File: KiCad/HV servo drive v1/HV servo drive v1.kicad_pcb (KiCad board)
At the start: 4 copper layers, 138.4 x 199.6 mm, 323 parts, among them J10 DC BUS J2, J3 PROG, J5 MOTOR, J6 PFC SENSE, J7 DC BUS J1, J8 8P8C_LED_Shielded_x2, J9 Conn_02x03_Top_Bottom, M1 Fan_4pin, M2 Fan_4pin, Q1 C3M0075120K, Q2 C3M0075120K, Q3 C3M0075120K, Q4 C3M0075120K, Q5 C3M0075120K, Q6 C3M0075120K, Q8 PMOS, SW1 SW_DIP_x04, SW2 TERM RES, U1 TCA9555PWR, U10 2EDF9275FXUMA1, U11 2EDF9275FXUMA1, U12 AMC1306M25DWVR, U13 2EDF9275FXUMA1, U14 AMC1306M25DWVR, U15 AMC1306M25DWVR, U16 6N137, U17 6N137, U18 FODM217A, U19 FODM217A, U2 ISO6721BQDRQ1, U20 WRF0505S-3WR2, U21 B0505MT-1WR4, U22 PL133-37TC, U23 THVD1552, U3 ISO6721BQDRQ1, U4 ISO6721BQDRQ1, U6 AP64060QWU-7, U7 WRF0505S-3WR2, U8 B0505MT-1WR4, U9 AP2127K-3.3, U9 STM32F413RGT6

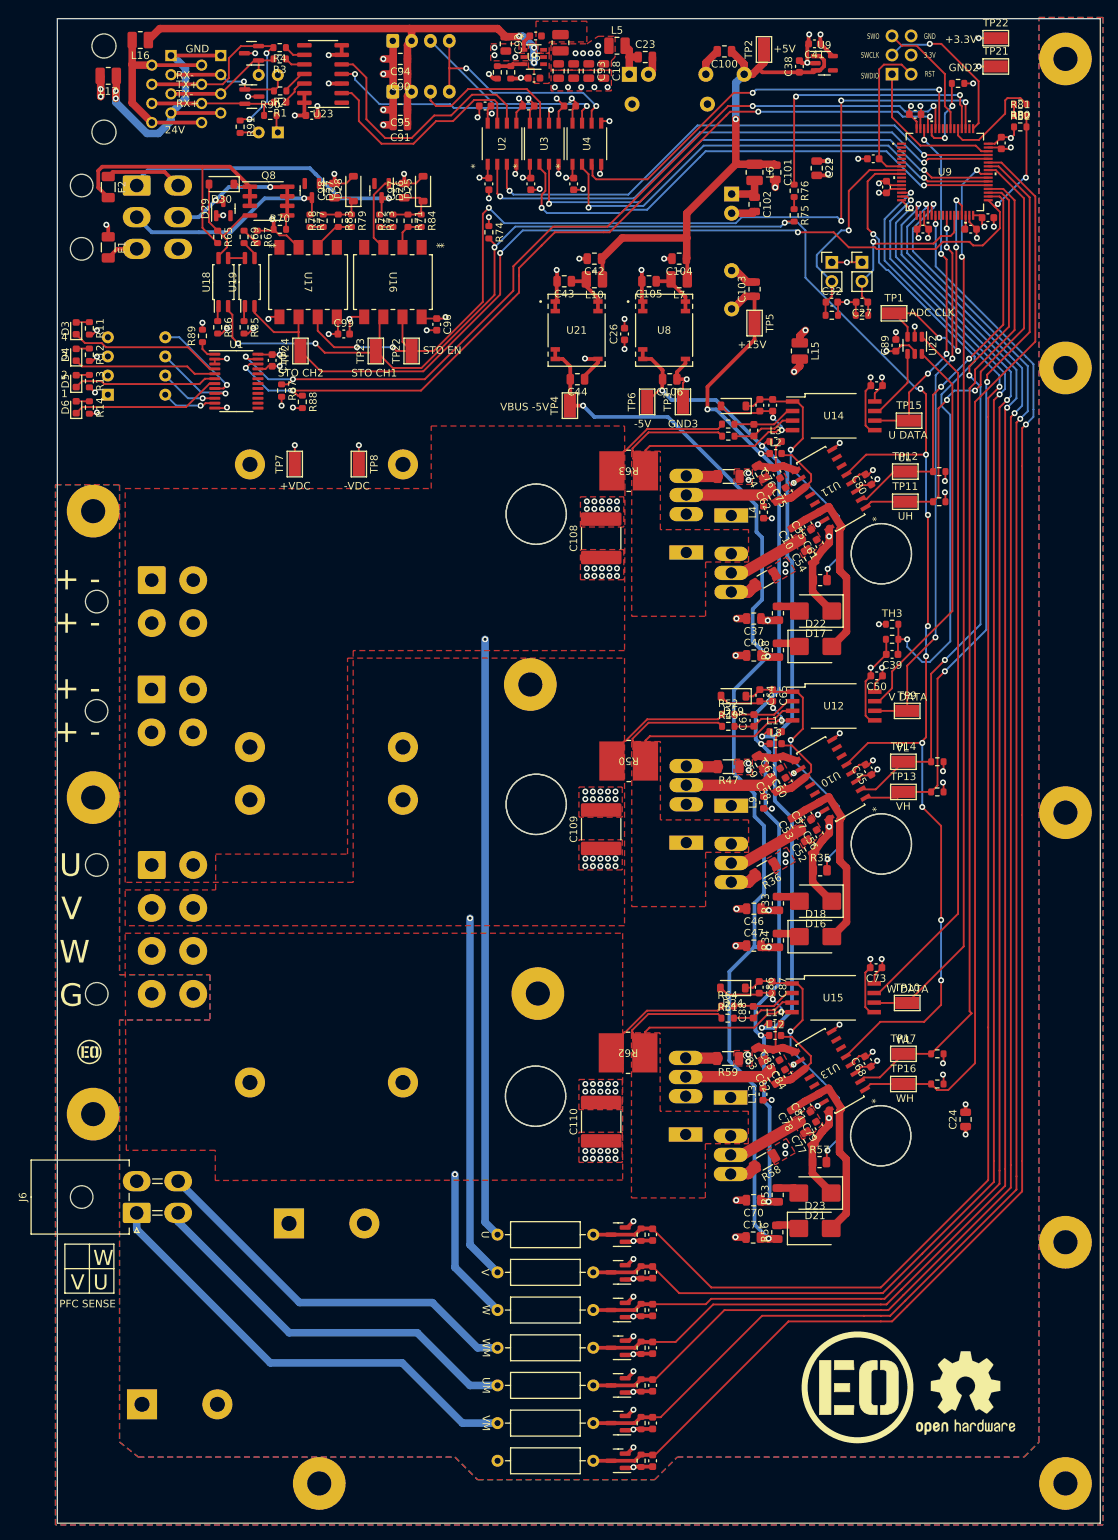
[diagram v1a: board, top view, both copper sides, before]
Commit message: start rev 2 changes
fix component references, fix rj45 and dc-dc converter footprints, add RLC filters on all power connectors, add more mounting holes
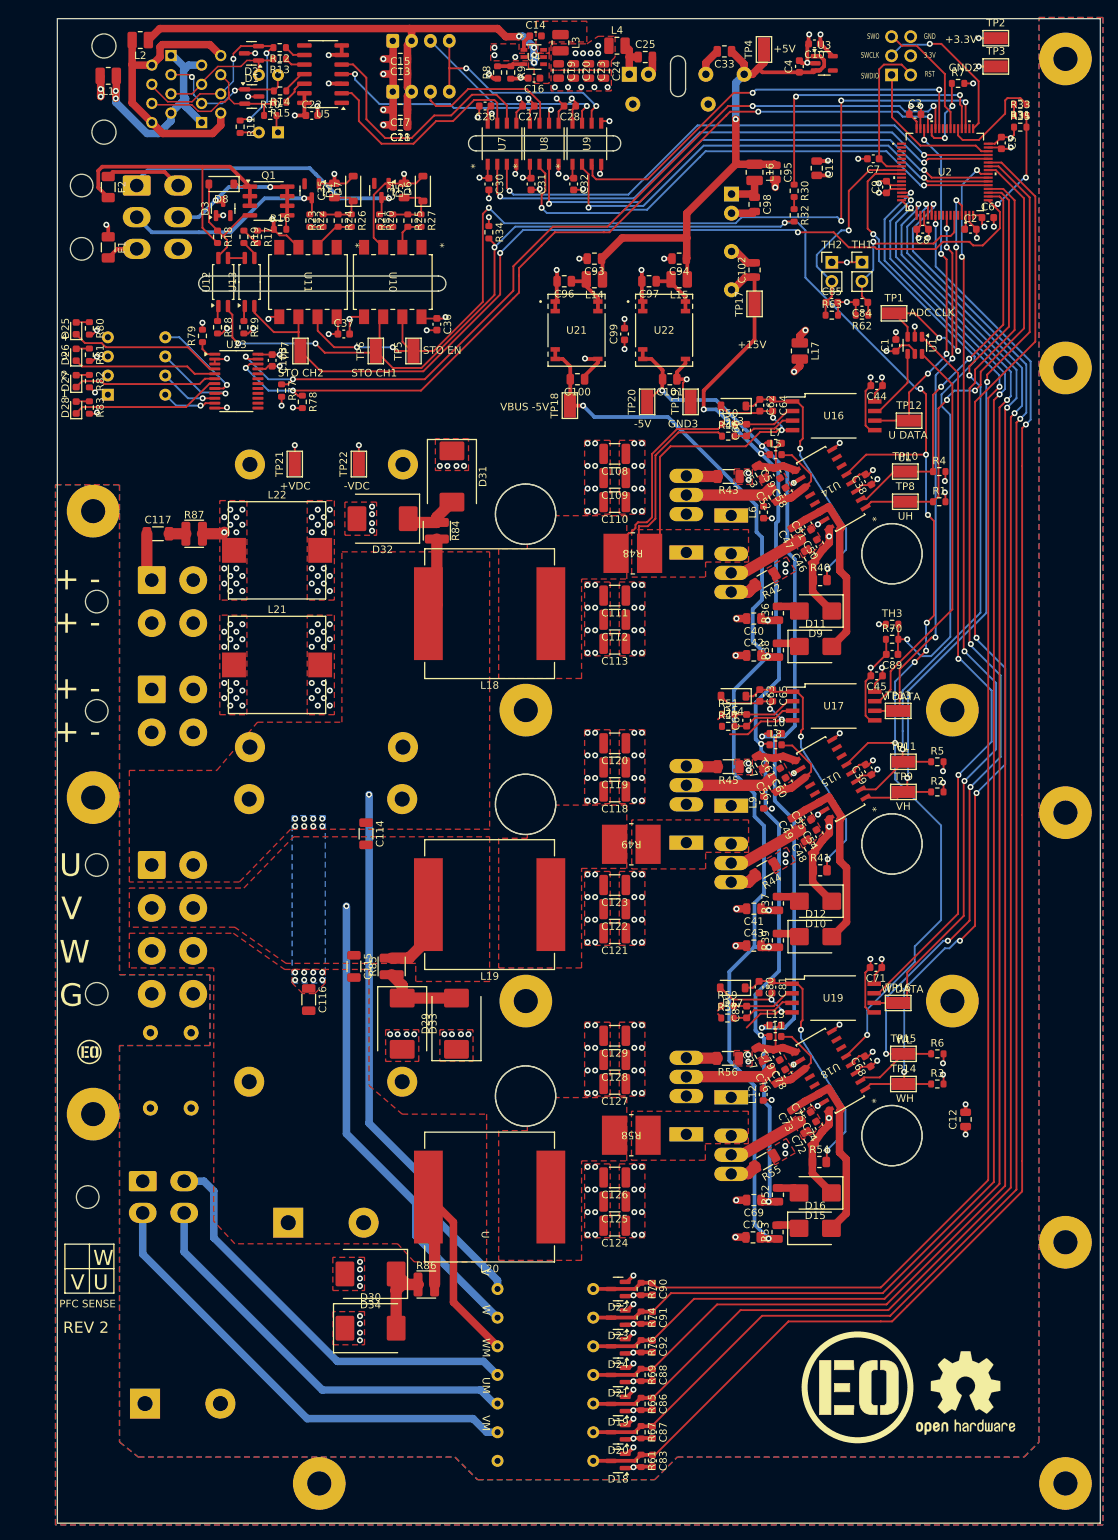
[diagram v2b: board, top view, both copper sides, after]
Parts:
- removed H14: MountingHole, footprints:MountingHole_3.2mm_M3_Pad_TopBottom_LargeIsolation
- removed J10: DC BUS J2, Connector_Molex:Molex_Mega-Fit_76825-0004_2x02_P5.70mm_Horizontal
- removed J8: 8P8C_LED_Shielded_x2, footprints:RJ45_E5908-0T0343-L
- removed J9: Conn_02x03_Top_Bottom, Connector_Molex:Molex_Mini-Fit_Jr_5569-06A2_2x03_P4.20mm_Horizontal
- removed Q8: PMOS, Package_SO:SOIC-8_3.9x4.9mm_P1.27mm
- removed R88, R89: 10k, Resistor_SMD:R_0603_1608Metric
- removed R90, R91: 120, Resistor_SMD:R_0603_1608Metric
- removed the REF** at (314.5, 188.8)
- removed the TP2 at (404.0, 55.8)
- removed TP23, TP24: TestPoint, footprints:TestPoint_Pad_3.1x1.6mm
- removed the TP3 at (393.2, 102.5)
- removed the U9 at (412.0, 57.6)
- removed the U9 at (428.0, 72.0)
- added C111: C, Capacitor_SMD:C_1210_3225Metric, F.Cu at (384.2, 128.2)
- added C112: C, Capacitor_SMD:C_1210_3225Metric, F.Cu at (384.2, 131.4)
- added C113: C, Capacitor_SMD:C_1210_3225Metric, F.Cu at (384.2, 134.6)
- added C114: 470pf, Capacitor_SMD:C_1206_3216Metric, F.Cu at (351.2, 159.8)
- added C115: 470pf, Capacitor_SMD:C_1206_3216Metric, F.Cu at (349.6, 177.4)
- added C116: 470pf, Capacitor_SMD:C_1206_3216Metric, F.Cu at (343.6, 181.8)
- added C117: 4.7nf, Capacitor_SMD:C_1206_3216Metric, F.Cu at (323.6, 120.0)
- added C118: C, Capacitor_SMD:C_1210_3225Metric, F.Cu at (384.2, 154.2)
- added C119: C, Capacitor_SMD:C_1210_3225Metric, F.Cu at (384.2, 151.0)
- added C120: C, Capacitor_SMD:C_1210_3225Metric, F.Cu at (384.2, 147.8)
- added C121: C, Capacitor_SMD:C_1210_3225Metric, F.Cu at (384.2, 173.0)
- added C122: C, Capacitor_SMD:C_1210_3225Metric, F.Cu at (384.2, 169.8)
- added C123: C, Capacitor_SMD:C_1210_3225Metric, F.Cu at (384.2, 166.6)
- added C124: C, Capacitor_SMD:C_1210_3225Metric, F.Cu at (384.2, 211.8)
- added C125: C, Capacitor_SMD:C_1210_3225Metric, F.Cu at (384.2, 208.6)
- added C126: C, Capacitor_SMD:C_1210_3225Metric, F.Cu at (384.2, 205.4)
- added C127: C, Capacitor_SMD:C_1210_3225Metric, F.Cu at (384.2, 193.0)
- added C128: C, Capacitor_SMD:C_1210_3225Metric, F.Cu at (384.2, 189.8)
- added C129: C, Capacitor_SMD:C_1210_3225Metric, F.Cu at (384.2, 186.6)
- added C130: 220pf, Capacitor_THT:C_Disc_D7.5mm_W5.0mm_P10.00mm, B.Cu at (328.0, 186.2)
- added C131: 220pf, Capacitor_THT:C_Disc_D7.5mm_W5.0mm_P10.00mm, B.Cu at (322.6, 186.2)
- added D11: D, Diode_SMD:D_SMB, F.Cu at (410.9, 134.9)
- added D31: D, Diode_SMD:D_SMC, F.Cu at (362.6, 112.4)
- added D32: D, Diode_SMD:D_SMC, F.Cu at (353.4, 118.0)
- added D33: D, Diode_SMD:D_SMC, F.Cu at (356.0, 185.0)
- added D34: D, Diode_SMD:D_SMC, F.Cu at (351.8, 218.2)
- added D7: BZT52C5V1, Diode_SMD:D_SOD-123, F.Cu at (349.5, 74.2)
- added H11: MountingHole, footprints:MountingHole_3.2mm_M3_Pad_TopBottom_LargeIsolation, F.Cu at (372.4, 182.0)
- added H2: MountingHole, footprints:MountingHole_3.2mm_M3_Pad_TopBottom_LargeIsolation, F.Cu at (444.0, 98.0)
- added H5: MountingHole, footprints:MountingHole_3.2mm_M3_Pad_TopBottom_LargeIsolation, F.Cu at (444.0, 246.0)
- added J1: PROG, Connector_PinHeader_2.54mm:PinHeader_2x03_P2.54mm_Vertical, B.Cu at (420.9, 59.1)
- added J2: 8P8C_LED_Shielded_x2, footprints:RJ45_E5908-0T0343-L, B.Cu at (316.4, 61.0)
- added J4: PFC SENSE, Connector_Molex:Molex_Mini-Fit_Jr_5569-04A2_2x02_P4.20mm_Horizontal, B.Cu at (321.6, 205.9)
- added L18: 1uH, Inductor_SMD:L_Vishay_IHLP-6767, F.Cu at (367.6, 130.6)
- added L19: 1uH, Inductor_SMD:L_Vishay_IHLP-6767, F.Cu at (367.6, 169.2)
- added L20: 1uH, Inductor_SMD:L_Vishay_IHLP-6767, F.Cu at (367.6, 208.0)
- added L21: 1uH, Inductor_SMD:L_Vishay_IHLP-5050, F.Cu at (339.4, 137.4)
- added L22: 1uH, Inductor_SMD:L_Vishay_IHLP-5050, F.Cu at (339.4, 122.2)
- added Q7: C3M0075120K, footprints:TO-247-4_Horizontal_TabUp, B.Cu at (393.7, 199.7)
- added R15: 10, Resistor_SMD:R_0603_1608Metric, F.Cu at (339.8, 62.8)
- added R16: 10K, Resistor_SMD:R_0603_1608Metric, F.Cu at (339.8, 79.6)
- added R17: 1K, Resistor_SMD:R_0603_1608Metric, F.Cu at (336.8, 80.6)
- added R31: 10K, Resistor_SMD:R_0603_1608Metric, F.Cu at (438.0, 63.0)
- added R32: 10K, Resistor_SMD:R_0603_1608Metric, F.Cu at (408.0, 77.8)
- added R7: 10k, Resistor_SMD:R_0603_1608Metric, F.Cu at (429.8, 60.2)
- added R8: 115k, Resistor_SMD:R_0603_1608Metric, F.Cu at (368.6, 58.8)
- added R9: 22.1k, Resistor_SMD:R_0603_1608Metric, F.Cu at (370.4, 58.8)
- added TP18: TestPoint, footprints:TestPoint_Pad_3.1x1.6mm, F.Cu at (378.2, 103.0)
- added TP19: TestPoint, footprints:TestPoint_Pad_3.1x1.6mm, F.Cu at (394.3, 102.5)
- added TP20: TestPoint, footprints:TestPoint_Pad_3.1x1.6mm, F.Cu at (388.5, 102.5)
- added TP21: TestPoint, footprints:TestPoint_Pad_3.1x1.6mm, F.Cu at (341.8, 110.8)
- added U5: THVD1552, Package_SO:SOIC-14_3.9x8.7mm_P1.27mm, F.Cu at (345.5, 59.0)
- added U9: ISO6721BQDRQ1, footprints:SOICN-8_LTF, F.Cu at (380.5, 68.2)
- C10, C16: value 10uf -> 2.2uf; footprint Capacitor_SMD:C_0805_2012Metric -> Capacitor_SMD:C_0603_1608Metric
- C103, C22, C37, C44, C54, C58, C59, C71, C74, C78, C83, C90, C91, C92: value 10uf -> 0.1uf; footprint Capacitor_SMD:C_0805_2012Metric -> Capacitor_SMD:C_0603_1608Metric
- C104, C105: value 10uf -> 470uf; footprint Capacitor_SMD:C_0805_2012Metric -> Capacitor_THT:CP_Radial_D30.0mm_P10.00mm_SnapIn; moved to B.Cu
- C106: value 10uf -> 40uf; footprint Capacitor_SMD:C_0805_2012Metric -> footprints:BUS CAP1; moved to B.Cu
- C107: value 0.1uf -> 40uf; footprint Capacitor_SMD:C_0603_1608Metric -> footprints:BUS CAP1; moved to B.Cu
- C108, C109, C110: value .1uf -> C; footprint Capacitor_SMD:C_2220_5650Metric -> Capacitor_SMD:C_1210_3225Metric
- C11, C25: value .1uf -> 10uf; footprint Capacitor_SMD:C_0603_1608Metric -> Capacitor_SMD:C_0805_2012Metric
- C12, C13, C41: value 2.2uf -> 10uf; footprint Capacitor_SMD:C_0603_1608Metric -> Capacitor_SMD:C_0805_2012Metric
- C14, C7: value 0.1uf -> .1uf
- C15, C17, C20, C21, C33, C34, C35, C56, C57, C69, C73, C76, C96: value 0.1uf -> 10uf; footprint Capacitor_SMD:C_0603_1608Metric -> Capacitor_SMD:C_0805_2012Metric
- C2, C4, C84, C85, C89: value 0.1uf -> 2.2uf
- C26: value 220pf -> 0.1uf
- C27, C32, C38, C39: value 2.2uf -> 0.1uf
- C29: value 0.1uf -> 220pf; footprint Capacitor_SMD:C_0603_1608Metric -> Capacitor_THT:C_Disc_D7.5mm_W5.0mm_P10.00mm; moved to B.Cu
- C31: value 220pf -> 0.1uf; footprint Capacitor_THT:C_Disc_D7.5mm_W5.0mm_P10.00mm -> Capacitor_SMD:C_0603_1608Metric; moved to F.Cu
- C48, C49: value 470uf -> 10uf; footprint Capacitor_THT:CP_Radial_D30.0mm_P10.00mm_SnapIn -> Capacitor_SMD:C_0805_2012Metric; moved to F.Cu
- C62: value 10uf -> 2.2; footprint Capacitor_SMD:C_0805_2012Metric -> Capacitor_SMD:C_0603_1608Metric
- C63, C80: value 0.1uf -> 2.2
- C64, C86: value 2.2 -> 0.1uf
- C66: value 2.2 -> C
- C72: value C -> 10uf; footprint Capacitor_SMD:C_0603_1608Metric -> Capacitor_SMD:C_0805_2012Metric
- C8, C9: value 40uf -> 0.1uf; footprint footprints:BUS CAP1 -> Capacitor_SMD:C_0603_1608Metric; moved to F.Cu
- C82: value 10uf -> C; footprint Capacitor_SMD:C_0805_2012Metric -> Capacitor_SMD:C_0603_1608Metric
- C88: value C -> 0.1uf
- C99: value 0.1uf -> 220pf
- D10, D12, D15, D9: value D_Dual_Series_ACK -> D; footprint Package_TO_SOT_SMD:SOT-23 -> Diode_SMD:D_SMB
- D13, D14, D8: value D_Dual_Series_ACK -> BZT52C5V1; footprint Package_TO_SOT_SMD:SOT-23 -> Diode_SMD:D_SOD-123
- D17: value D -> BZT52C5V1; footprint Diode_SMD:D_SMB -> Diode_SMD:D_SOD-123
- D18, D21, D22, D23: value D -> D_Dual_Series_ACK; footprint Diode_SMD:D_SMB -> Package_TO_SOT_SMD:SOT-23
- D19, D20, D24: value BZT52C5V1 -> D_Dual_Series_ACK; footprint Diode_SMD:D_SOD-123 -> Package_TO_SOT_SMD:SOT-23
- D25, D28: value BZT52C5V1 -> LED; footprint Diode_SMD:D_SOD-123 -> LED_SMD:LED_0603_1608Metric
- D26, D27: value D_Dual_Series_ACK -> LED; footprint Package_TO_SOT_SMD:SOT-23 -> LED_SMD:LED_0603_1608Metric
- D29: value D_Dual_Series_ACK -> D; footprint Package_TO_SOT_SMD:SOT-23 -> Diode_SMD:D_SMC
- D3, D4, D5: value LED -> D_Dual_Series_ACK; footprint LED_SMD:LED_0603_1608Metric -> Package_TO_SOT_SMD:SOT-23
- D30: value BZT52C5V1 -> D; footprint Diode_SMD:D_SOD-123 -> Diode_SMD:D_SMC
- D6: value LED -> BZT52C5V1; footprint LED_SMD:LED_0603_1608Metric -> Diode_SMD:D_SOD-123
- J3: value PROG -> Conn_02x03_Top_Bottom; footprint Connector_PinHeader_2.54mm:PinHeader_2x03_P2.54mm_Vertical -> Connector_Molex:Molex_Mini-Fit_Jr_5569-06A2_2x03_P4.20mm_Horizontal
- J6: value PFC SENSE -> DC BUS J1; footprint Connector_Molex:Molex_Mini-Fit_Jr_5569-04A2_2x02_P4.20mm_Horizontal -> Connector_Molex:Molex_Mega-Fit_76825-0004_2x02_P5.70mm_Horizontal; moved to B.Cu
- J7: value DC BUS J1 -> DC BUS J2
- L10, L5, L6, L7: footprint Inductor_SMD:L_1008_2520Metric -> Inductor_SMD:L_0603_1608Metric
- L14, L2, L3, L4: footprint Inductor_SMD:L_0603_1608Metric -> Inductor_SMD:L_1008_2520Metric
- Q1: value C3M0075120K -> PMOS; footprint footprints:TO-247-4_Horizontal_TabUp -> Package_SO:SOIC-8_3.9x4.9mm_P1.27mm; moved to F.Cu
- R1, R2, R3, R4: value 10 -> 10k
- R10: value 10k -> 120
- R11: value 1k -> 120
- R12, R13, R14: value 1k -> 10
- R18: value 10k -> 10K
- R19, R20, R21, R22, R23: value 10k -> 1K
- R24: value 10k -> 1k
- R25, R27: value 1M -> 1k; footprint Resistor_THT:R_Axial_DIN0309_L9.0mm_D3.2mm_P12.70mm_Horizontal -> Resistor_SMD:R_0603_1608Metric
- R26: value 5k -> 1k
- R28: value 5k -> 220
- R29: value 1M -> 220; footprint Resistor_THT:R_Axial_DIN0309_L9.0mm_D3.2mm_P12.70mm_Horizontal -> Resistor_SMD:R_0603_1608Metric
- R30: value 5k -> 10K
- R33: value 1 -> 10K; footprint Resistor_SMD:R_0805_2012Metric -> Resistor_SMD:R_0603_1608Metric
- R34: value 1 -> 1K; footprint Resistor_SMD:R_0805_2012Metric -> Resistor_SMD:R_0603_1608Metric
- R35: value 800 -> 1K; footprint Resistor_SMD:R_0805_2012Metric -> Resistor_SMD:R_0603_1608Metric
- R36: value 10 -> 1; footprint Resistor_SMD:R_1206_3216Metric -> Resistor_SMD:R_0805_2012Metric
- R37: value 10k -> 1; footprint Resistor_SMD:R_0603_1608Metric -> Resistor_SMD:R_0805_2012Metric
- R38: value 1M -> 1; footprint Resistor_THT:R_Axial_DIN0309_L9.0mm_D3.2mm_P12.70mm_Horizontal -> Resistor_SMD:R_0805_2012Metric
- R39: value 5k -> 1; footprint Resistor_SMD:R_0603_1608Metric -> Resistor_SMD:R_0805_2012Metric
- R40: value 1M -> 800; footprint Resistor_THT:R_Axial_DIN0309_L9.0mm_D3.2mm_P12.70mm_Horizontal -> Resistor_SMD:R_0805_2012Metric
- R41: value 5k -> 800; footprint Resistor_SMD:R_0603_1608Metric -> Resistor_SMD:R_0805_2012Metric
- R42, R44: value 1M -> 10; footprint Resistor_THT:R_Axial_DIN0309_L9.0mm_D3.2mm_P12.70mm_Horizontal -> Resistor_SMD:R_1206_3216Metric
- R43, R45: value 5k -> 10; footprint Resistor_SMD:R_0603_1608Metric -> Resistor_SMD:R_1206_3216Metric
- R46: value 10k -> R
- R47, R59: value 10 -> R; footprint Resistor_SMD:R_1206_3216Metric -> Resistor_SMD:R_0603_1608Metric
- R48: value 1 -> .005; footprint Resistor_SMD:R_0805_2012Metric -> footprints:RES_HCSM2818_STP
- R49: value R -> .005; footprint Resistor_SMD:R_0603_1608Metric -> footprints:RES_HCSM2818_STP
- R5: value 115k -> 10k
- R50: value .005 -> R; footprint footprints:RES_HCSM2818_STP -> Resistor_SMD:R_0603_1608Metric
- R51, R57: value 800 -> R; footprint Resistor_SMD:R_0805_2012Metric -> Resistor_SMD:R_0603_1608Metric
- R52: value R -> 1; footprint Resistor_SMD:R_0603_1608Metric -> Resistor_SMD:R_0805_2012Metric
- R54: value 10 -> 800; footprint Resistor_SMD:R_1206_3216Metric -> Resistor_SMD:R_0805_2012Metric
- R56: value 1 -> 10; footprint Resistor_SMD:R_0805_2012Metric -> Resistor_SMD:R_1206_3216Metric
- R58: value 10 -> .005; footprint Resistor_SMD:R_1206_3216Metric -> footprints:RES_HCSM2818_STP
- R6: value 22.1k -> 10k
- R60, R64, R66: value R -> 1M; footprint Resistor_SMD:R_0603_1608Metric -> Resistor_THT:R_Axial_DIN0309_L9.0mm_D3.2mm_P12.70mm_Horizontal; moved to B.Cu
- R61: value R -> 5k
- R62, R63: value .005 -> 10k; footprint footprints:RES_HCSM2818_STP -> Resistor_SMD:R_0603_1608Metric
- R65, R76: value 10K -> 5k
- R67, R69, R72, R74: value 1K -> 5k
- R68: value 1 -> 1M; footprint Resistor_SMD:R_0805_2012Metric -> Resistor_THT:R_Axial_DIN0309_L9.0mm_D3.2mm_P12.70mm_Horizontal; moved to B.Cu
- R70: value 10K -> 10k
- R71: value 1k -> 1M; footprint Resistor_SMD:R_0603_1608Metric -> Resistor_THT:R_Axial_DIN0309_L9.0mm_D3.2mm_P12.70mm_Horizontal; moved to B.Cu
- R73: value 1K -> 1M; footprint Resistor_SMD:R_0603_1608Metric -> Resistor_THT:R_Axial_DIN0309_L9.0mm_D3.2mm_P12.70mm_Horizontal; moved to B.Cu
- R75: value 10K -> 1M; footprint Resistor_SMD:R_0603_1608Metric -> Resistor_THT:R_Axial_DIN0309_L9.0mm_D3.2mm_P12.70mm_Horizontal; moved to B.Cu
- R77, R78: value 1K -> 10k
- R79: value 1k -> 10k
- R80, R81: value 10K -> 1k
- R82: value 1K -> 1k
- R84: value 1k -> 4.7; footprint Resistor_SMD:R_0603_1608Metric -> footprints:R_1206_3216Metric_Wide
- R85, R86: value 220 -> 4.7; footprint Resistor_SMD:R_0603_1608Metric -> footprints:R_1206_3216Metric_Wide
- R87: value 10k -> 4.7; footprint Resistor_SMD:R_0603_1608Metric -> footprints:R_1206_3216Metric_Wide
- SW1: value SW_DIP_x04 -> TERM RES; footprint Package_DIP:DIP-8_W7.62mm -> Package_DIP:DIP-4_W7.62mm
- SW2: value TERM RES -> SW_DIP_x04; footprint Package_DIP:DIP-4_W7.62mm -> Package_DIP:DIP-8_W7.62mm
- U1: value TCA9555PWR -> PL133-37TC; footprint Package_SO:TSSOP-24_4.4x7.8mm_P0.65mm -> Package_TO_SOT_SMD:SOT-23-6
- U10, U11: value 2EDF9275FXUMA1 -> 6N137; footprint footprints:PG-DSO-16-11 -> footprints:6N137S_LTO
- U12: value AMC1306M25DWVR -> FODM217A; footprint footprints:DWV0008A -> Package_SO:SOP-4_4.4x2.6mm_P1.27mm
- U13: value 2EDF9275FXUMA1 -> FODM217A; footprint footprints:PG-DSO-16-11 -> Package_SO:SOP-4_4.4x2.6mm_P1.27mm
- U14, U15: value AMC1306M25DWVR -> 2EDF9275FXUMA1; footprint footprints:DWV0008A -> footprints:PG-DSO-16-11
- U16, U17: value 6N137 -> AMC1306M25DWVR; footprint footprints:6N137S_LTO -> footprints:DWV0008A
- U18: value FODM217A -> 2EDF9275FXUMA1; footprint Package_SO:SOP-4_4.4x2.6mm_P1.27mm -> footprints:PG-DSO-16-11
- U19: value FODM217A -> AMC1306M25DWVR; footprint Package_SO:SOP-4_4.4x2.6mm_P1.27mm -> footprints:DWV0008A
- U2: value ISO6721BQDRQ1 -> STM32F413RGT6; footprint footprints:SOICN-8_LTF -> footprints:LQFP64-10x10mm
- U20: footprint footprints:F0505S-2WR3 -> footprints:B0515
- U22: value PL133-37TC -> B0505MT-1WR4; footprint Package_TO_SOT_SMD:SOT-23-6 -> footprints:B05xxMT-1WR4_MNS
- U23: value THVD1552 -> TCA9555PWR; footprint Package_SO:SOIC-14_3.9x8.7mm_P1.27mm -> Package_SO:TSSOP-24_4.4x7.8mm_P0.65mm
- U3: value ISO6721BQDRQ1 -> AP2127K-3.3; footprint footprints:SOICN-8_LTF -> Package_TO_SOT_SMD:SOT-23-5
- U4: value ISO6721BQDRQ1 -> AP64060QWU-7; footprint footprints:SOICN-8_LTF -> footprints:IC6_AP64060QWU-7_DIO
- U6: value AP64060QWU-7 -> WRF0505S-3WR2; footprint footprints:IC6_AP64060QWU-7_DIO -> footprints:F0505S-2WR3; moved to B.Cu
- U7: value WRF0505S-3WR2 -> ISO6721BQDRQ1; footprint footprints:F0505S-2WR3 -> footprints:SOICN-8_LTF; moved to F.Cu
- U8: value B0505MT-1WR4 -> ISO6721BQDRQ1; footprint footprints:B05xxMT-1WR4_MNS -> footprints:SOICN-8_LTF
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- renumbered TP22 to TP2, TP21 to TP3
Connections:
- C1 pad 1: 5v_ISO -> +3.3V
- C1 pad 2: GND1 -> GND2
- C10 pad 1: Net-(Q3-DS) -> +3.3V
- C10 pad 2: Net-(D22-A) -> GND2
- C100 pad 1: +5V -> +VDC
- C100 pad 2: GND2 -> VBUS -5V
- C101 pad 1: +5V -> GND3
- C101 pad 2: GND2 -> -5V
- C102 pad 1: Net-(U20-VIN) -> +15V
- C102 pad 2: GND2 -> GND3
- C103 pad 1: +15V -> +3.3V
- C103 pad 2: GND3 -> GND2
- C104 pad 1: +5V -> +VDC
- C104 pad 2: GND2 -> -VDC
- C105 pad 1: Net-(C105-Pad1) -> +VDC
- C105 pad 2: GND2 -> -VDC
- C106 pad 1: GND3 -> +VDC
- C106 pad 2: -5V -> -VDC
- C107 pad 1: +3.3V -> +VDC
- C107 pad 2: GND2 -> -VDC
- C108 pad 1: -VDC -> +VDC
- C108 pad 2: +VDC -> -VDC
- C109 pad 1: -VDC -> +VDC
- C109 pad 2: +VDC -> -VDC
- C11 pad 1: Net-(U6-BST) -> +3.3V
- C11 pad 2: Net-(U6-SW) -> GND2
- C110 pad 1: -VDC -> +VDC
- C110 pad 2: +VDC -> -VDC
- C12 pad 1: Net-(U5A-VCAP_1) -> +3.3V
- C14 pad 1: +3.3V -> Net-(U4-BST)
- C14 pad 2: GND2 -> Net-(U4-SW)
- C15 pad 1: +3.3V -> 24V_ISO
- C15 pad 2: GND2 -> GND1
- C16 pad 1: 5v_ISO -> 24V_ISO
- C17 pad 1: +3.3V -> 24V_ISO
- C17 pad 2: GND2 -> GND1
- C18 pad 1: 5v_ISO -> 24V_ISO
- C2 pad 1: 5v_ISO -> Net-(U2A-VCAP_1)
- C2 pad 2: GND1 -> GND2
- C20 pad 1: +3.3V -> 5v_ISO
- C20 pad 2: GND2 -> GND1
- C21 pad 1: +3.3V -> 24V_ISO
- C21 pad 2: GND2 -> GND1
- C22 pad 1: +3.3V -> 5v_ISO
- C22 pad 2: GND2 -> GND1
- C23 pad 1: Net-(U7-VIN) -> 5v_ISO
- C24 pad 1: +3.3V -> 5v_ISO
- C24 pad 2: GND2 -> GND1
- C25 pad 1: RESET -> Net-(U6-VIN)
- C25 pad 2: GND2 -> GND1
- C26 pad 1: GND3 -> 5v_ISO
- C26 pad 2: GND2 -> GND1
- C27 pad 1: HEATSINK_TEMP_1_ADC -> 5v_ISO
- C27 pad 2: GND2 -> GND1
- C28 pad 1: UM_ADC -> 5v_ISO
- C28 pad 2: GND2 -> GND1
- C29 pad 1: VM_ADC -> GND2
- C29 pad 2: GND2 -> GND1
- C3 pad 1: 5v_ISO -> +3.3V
- C3 pad 2: GND1 -> GND2
- C30 pad 1: WM_ADC -> +3.3V
- C31 pad 1: GND2 -> +3.3V
- C31 pad 2: GND1 -> GND2
- C32 pad 1: HEATSINK_TEMP_2_ADC -> +3.3V
- C33 pad 1: U_ADC -> +5V
- C34 pad 1: V_ADC -> Net-(D6-K)
- C34 pad 2: GND2 -> SAFE GND
- C35 pad 1: W_ADC -> Net-(D7-K)
- C35 pad 2: GND2 -> SAFE GND
- C36 pad 1: VBUS_ADC -> +3.3V
- C37 pad 1: +15V -> +3.3V
- C37 pad 2: GND3 -> GND2
- C38 pad 1: +5V -> +3.3V
- C39 pad 1: BOARD_TEMP_1_ADC -> +3.3V
- C4 pad 1: 5v_ISO -> +5V
- C4 pad 2: GND1 -> GND2
- C40 pad 1: +VDC -> +15V
- C40 pad 2: VBUS -5V -> GND3
- C41 pad 1: +3.3V -> +15V
- C41 pad 2: GND2 -> GND3
- C42 pad 1: +5V -> +VDC
- C42 pad 2: GND2 -> VBUS -5V
- C43 pad 1: Net-(C43-Pad1) -> +VDC
- C43 pad 2: GND2 -> VBUS -5V
- C44 pad 1: +VDC -> +3.3V
- C44 pad 2: VBUS -5V -> GND2
- C46 pad 1: +15V -> Net-(D9-K)
- C46 pad 2: GND3 -> Net-(Q2-DS)
- C47 pad 1: +VDC -> Net-(Q2-DS)
- C47 pad 2: VBUS -5V -> Net-(D11-A)
- C48 pad 1: +VDC -> Net-(D10-K)
- C48 pad 2: -VDC -> Net-(Q4-DS)
- C49 pad 1: +VDC -> Net-(Q4-DS)
- C49 pad 2: -VDC -> Net-(D12-A)
- C50 pad 1: +3.3V -> Net-(D9-K)
- C50 pad 2: GND2 -> Net-(Q2-DS)
- C51 pad 1: +3.3V -> Net-(Q2-DS)
- C51 pad 2: GND2 -> Net-(D11-A)
- C52 pad 1: Net-(D16-K) -> Net-(U14-VDDB)
- C52 pad 2: Net-(Q1-DS) -> Net-(Q3-DS)
- C53 pad 1: Net-(Q1-DS) -> Net-(Q3-DS)
- C53 pad 2: Net-(D18-A) -> Net-(U14-GNDB)
- C54 pad 1: Net-(D17-K) -> Net-(D10-K)
- C54 pad 2: Net-(Q3-DS) -> Net-(Q4-DS)
- C55 pad 1: Net-(Q3-DS) -> Net-(Q4-DS)
- C55 pad 2: Net-(D22-A) -> Net-(D12-A)
- C56 pad 1: Net-(D16-K) -> Net-(U15-VDDB)
- C56 pad 2: Net-(Q1-DS) -> Net-(Q5-DS)
- C57 pad 1: Net-(Q1-DS) -> Net-(Q5-DS)
- C57 pad 2: Net-(D18-A) -> Net-(U15-GNDB)
- C58 pad 1: Net-(U10-VDDB) -> Net-(U14-VDDB)
- C58 pad 2: Net-(Q2-DS) -> Net-(Q3-DS)
- C59 pad 1: Net-(Q2-DS) -> Net-(Q3-DS)
- C59 pad 2: Net-(U10-GNDB) -> Net-(U14-GNDB)
- C60 pad 1: Net-(U10-VDDB) -> Net-(U15-VDDB)
- C60 pad 2: Net-(Q2-DS) -> Net-(Q5-DS)
- C61 pad 1: Net-(D17-K) -> Net-(Q5-DS)
- C61 pad 2: Net-(Q3-DS) -> Net-(U15-GNDB)
- C62 pad 1: Net-(U11-VDDB) -> Net-(D13-K)
- C62 pad 2: Net-(Q4-DS) -> Net-(D13-A)
- C63 pad 1: Net-(Q2-DS) -> Net-(D14-K)
- C63 pad 2: Net-(U10-GNDB) -> Net-(D14-A)
- C64 pad 1: Net-(D19-K) -> Net-(D13-K)
- C64 pad 2: Net-(D19-A) -> Net-(D13-A)
- C65 pad 1: Net-(D19-K) -> Net-(D14-K)
- C65 pad 2: Net-(D19-A) -> Net-(D14-A)
- C66 pad 1: Net-(D20-K) -> Net-(U16-AINN)
- C66 pad 2: Net-(D20-A) -> Net-(U16-AINP)
- C67 pad 1: Net-(U12-AINN) -> Net-(U17-AINN)
- C67 pad 2: Net-(U12-AINP) -> Net-(U17-AINP)
- C69 pad 1: Net-(D20-K) -> +15V
- C69 pad 2: Net-(D20-A) -> GND3
- C7 pad 1: +3.3V -> RESET
- C70 pad 1: +15V -> +VDC
- C70 pad 2: GND3 -> VBUS -5V
- C71 pad 1: +VDC -> +3.3V
- C71 pad 2: VBUS -5V -> GND2
- C72 pad 1: Net-(U14-AINN) -> Net-(D15-K)
- C72 pad 2: Net-(U14-AINP) -> Net-(Q6-DS)
- C73 pad 1: +3.3V -> Net-(Q6-DS)
- C73 pad 2: GND2 -> Net-(D16-A)
- C74 pad 1: Net-(Q4-DS) -> Net-(D15-K)
- C74 pad 2: Net-(U11-GNDB) -> Net-(Q6-DS)
- C75 pad 1: Net-(U11-VDDB) -> Net-(Q6-DS)
- C75 pad 2: Net-(Q4-DS) -> Net-(D16-A)
- C76 pad 1: Net-(Q4-DS) -> Net-(U18-VDDB)
- C76 pad 2: Net-(U11-GNDB) -> Net-(Q7-DS)
- C77 pad 1: Net-(D21-K) -> Net-(Q7-DS)
- C77 pad 2: Net-(Q5-DS) -> Net-(U18-GNDB)
- C78 pad 1: Net-(Q5-DS) -> Net-(U18-VDDB)
- C78 pad 2: Net-(D23-A) -> Net-(Q7-DS)
- C79 pad 1: Net-(D21-K) -> Net-(Q7-DS)
- C79 pad 2: Net-(Q5-DS) -> Net-(U18-GNDB)
- C8 pad 1: +VDC -> +3.3V
- C8 pad 2: -VDC -> GND2
- C80 pad 1: +3.3V -> Net-(D17-K)
- C80 pad 2: GND2 -> Net-(D17-A)
- C81 pad 1: Net-(Q5-DS) -> Net-(D17-K)
- C81 pad 2: Net-(D23-A) -> Net-(D17-A)
- C82 pad 1: Net-(U13-VDDB) -> Net-(U19-AINN)
- C82 pad 2: Net-(Q6-DS) -> Net-(U19-AINP)
- C83 pad 1: Net-(Q6-DS) -> VBUS_ADC
- C83 pad 2: Net-(U13-GNDB) -> GND2
- C84 pad 1: Net-(U13-VDDB) -> HEATSINK_TEMP_1_ADC
- C84 pad 2: Net-(Q6-DS) -> GND2
- C85 pad 1: Net-(Q6-DS) -> HEATSINK_TEMP_2_ADC
- C85 pad 2: Net-(U13-GNDB) -> GND2
- C86 pad 1: Net-(D24-K) -> UM_ADC
- C86 pad 2: Net-(D24-A) -> GND2
- C87 pad 1: Net-(D24-K) -> VM_ADC
- C87 pad 2: Net-(D24-A) -> GND2
- C88 pad 1: Net-(U15-AINN) -> WM_ADC
- C88 pad 2: Net-(U15-AINP) -> GND2
- C89 pad 1: +3.3V -> BOARD_TEMP_1_ADC
- C9 pad 1: +VDC -> +3.3V
- C9 pad 2: -VDC -> GND2
- C90 pad 1: 24V_ISO -> U_ADC
- C90 pad 2: GND1 -> GND2
- C91 pad 1: 24V_ISO -> V_ADC
- C91 pad 2: GND1 -> GND2
- C92 pad 1: 24V_ISO -> W_ADC
- C92 pad 2: GND1 -> GND2
- C93 pad 1: 5v_ISO -> +5V
- C93 pad 2: GND1 -> GND2
- C94 pad 1: 24V_ISO -> +5V
- C94 pad 2: GND1 -> GND2
- C95 pad 1: 24V_ISO -> +5V
- C95 pad 2: GND1 -> GND2
- C96 pad 1: +3.3V -> Net-(C96-Pad1)
- C97 pad 1: Net-(D25-K) -> Net-(C97-Pad1)
- C97 pad 2: SAFE GND -> GND2
- C98 pad 1: Net-(D28-K) -> Net-(U20-VIN)
- C98 pad 2: SAFE GND -> GND2
- C99 pad 1: +3.3V -> GND3
- D10 pad 1: GND2 -> Net-(D10-K)
- D10 pad 2: +3.3V -> Net-(D10-A)
- D12 pad 1: GND2 -> Net-(D12-K)
- D12 pad 2: +3.3V -> Net-(D12-A)
- D13 pad 1: GND2 -> Net-(D13-K)
- D13 pad 2: +3.3V -> Net-(D13-A)
- D14 pad 1: GND2 -> Net-(D14-K)
- D14 pad 2: +3.3V -> Net-(D14-A)
- D15 pad 1: GND2 -> Net-(D15-K)
- D15 pad 2: +3.3V -> Net-(D15-A)
- D18 pad 1: Net-(D18-K) -> GND2
- D18 pad 2: Net-(D18-A) -> +3.3V
- D19 pad 1: Net-(D19-K) -> GND2
- D19 pad 2: Net-(D19-A) -> +3.3V
- D20 pad 1: Net-(D20-K) -> GND2
- D20 pad 2: Net-(D20-A) -> +3.3V
- D21 pad 1: Net-(D21-K) -> GND2
- D21 pad 2: Net-(D21-A) -> +3.3V
- D22 pad 1: Net-(D22-K) -> GND2
- D22 pad 2: Net-(D22-A) -> +3.3V
- D23 pad 1: Net-(D23-K) -> GND2
- D23 pad 2: Net-(D23-A) -> +3.3V
- D24 pad 1: Net-(D24-K) -> GND2
- D24 pad 2: Net-(D24-A) -> +3.3V
- D25 pad 2: SAFE GND -> Net-(D25-A)
- D26 pad 1: SAFE GND -> Net-(D26-K)
- D26 pad 2: unconnected-(D26-K-Pad2) -> Net-(D26-A)
- D27 pad 1: SAFE GND -> Net-(D27-K)
- D27 pad 2: unconnected-(D27-K-Pad2) -> Net-(D27-A)
- D28 pad 2: SAFE GND -> Net-(D28-A)
- D29 pad 1: SAFE GND -> +VDC
- D29 pad 2: unconnected-(D29-K-Pad2) -> Net-(D29-A)
- D3 pad 1: Net-(D3-K) -> SAFE GND
- D3 pad 2: Net-(D3-A) -> unconnected-(D3-K-Pad2)
- D30 pad 1: STO FBK 24V -> +VDC
- D4 pad 1: Net-(D4-K) -> SAFE GND
- D4 pad 2: Net-(D4-A) -> unconnected-(D4-K-Pad2)
- D5 pad 1: Net-(D5-K) -> SAFE GND
- D5 pad 2: Net-(D5-A) -> unconnected-(D5-K-Pad2)
- D6 pad 2: Net-(D6-A) -> SAFE GND
- D8 pad 1: GND2 -> STO FBK 24V
- D8 pad 2: +3.3V -> Net-(D8-A)
- D9 pad 1: GND2 -> Net-(D9-K)
- D9 pad 2: +3.3V -> Net-(D9-A)
- F1 pad 2: Net-(J9-Pin_3) -> Net-(J3-Pin_3)
- F2 pad 1: Net-(J9-Pin_4) -> Net-(J3-Pin_4)
- H10 pad 1: GND -> (no net)
- H12 pad 1: GND -> (no net)
- H13 pad 1: GND -> (no net)
- H3 pad 1: (no net) -> GND
- H8 pad 1: (no net) -> GND
- J3 pad 1: SWDIO -> STO CH1 FIELD
- J3 pad 2: RESET -> STO CH2 FIELD
- J3 pad 3: SWCLK -> Net-(J3-Pin_3)
- J3 pad 4: +3.3V -> Net-(J3-Pin_4)
- J3 pad 5: SWO -> STO FBK OUT
- J3 pad 6: GND2 -> unconnected-(J3-Pin_6-Pad6)
- J6 pad 1: VM -> DCBUS+
- J6 pad 2: unconnected-(J6-Pin_2-Pad2) -> DCBUS+
- J6 pad 3: UM -> DCBUS-
- J6 pad 4: WM -> DCBUS-
- J7 pad 1: +VDC -> DCBUS+
- J7 pad 2: +VDC -> DCBUS+
- J7 pad 3: -VDC -> DCBUS-
- J7 pad 4: -VDC -> DCBUS-
- L1 pad 1: Net-(U6-SW) -> Net-(J2-Pad14)
- L1 pad 2: 5v_ISO -> GND1
- L10 pad 1: +5V -> -5V
- L10 pad 2: Net-(C43-Pad1) -> Net-(U15-GNDB)
- L11 pad 1: -5V -> +15V
- L11 pad 2: Net-(U10-GNDB) -> Net-(U18-VDDB)
- L12 pad 1: +15V -> GND3
- L12 pad 2: Net-(U13-VDDB) -> Net-(Q7-DS)
- L13 pad 1: GND3 -> -5V
- L13 pad 2: Net-(Q6-DS) -> Net-(U18-GNDB)
- L14 pad 1: -5V -> +5V
- L14 pad 2: Net-(U13-GNDB) -> Net-(C96-Pad1)
- L15 pad 1: GND2 -> +5V
- L15 pad 2: GND3 -> Net-(C97-Pad1)
- L16 pad 1: 24V_ISO -> +5V
- L16 pad 2: Net-(J8-Pad1) -> Net-(U20-VIN)
- L17 pad 1: Net-(J8-Pad14) -> GND2
- L17 pad 2: GND1 -> GND3
- L2 pad 1: +15V -> 24V_ISO
- L2 pad 2: Net-(U11-VDDB) -> Net-(J2-Pad1)
- L3 pad 1: -5V -> Net-(U4-SW)
- L3 pad 2: Net-(U11-GNDB) -> 5v_ISO
- L4 pad 1: GND3 -> 5v_ISO
- L4 pad 2: Net-(Q4-DS) -> Net-(U6-VIN)
- L5 pad 1: 5v_ISO -> +15V
- L5 pad 2: Net-(U7-VIN) -> Net-(U14-VDDB)
- L6 pad 1: +5V -> GND3
- L6 pad 2: Net-(U20-VIN) -> Net-(Q3-DS)
- L7 pad 1: +5V -> -5V
- L7 pad 2: Net-(C105-Pad1) -> Net-(U14-GNDB)
- L8 pad 2: Net-(U10-VDDB) -> Net-(U15-VDDB)
- L9 pad 2: Net-(Q2-DS) -> Net-(Q5-DS)
- M1 pad 3: TACH_1_ISO -> TACH_2_ISO
- M2 pad 3: TACH_2_ISO -> TACH_1_ISO
- Q1 pad 1: +VDC -> STO FBK 24V
- Q1 pad 2: Net-(D19-A) -> STO FBK 24V
- Q1 pad 3: Net-(Q1-DS) -> STO FBK 24V
- Q1 pad 4: Net-(Q1-G) -> Net-(D8-A)
- Q2 pad 1: Net-(D19-A) -> +VDC
- Q2 pad 2: -VDC -> Net-(D13-A)
- Q3 pad 1: +VDC -> Net-(D13-A)
- Q3 pad 2: Net-(D20-A) -> -VDC
- Q4 pad 1: Net-(D20-A) -> +VDC
- Q4 pad 2: -VDC -> Net-(D14-A)
- Q5 pad 1: +VDC -> Net-(D14-A)
- Q5 pad 2: Net-(D24-A) -> -VDC
- Q6 pad 1: Net-(D24-A) -> +VDC
- Q6 pad 2: -VDC -> Net-(D17-A)
- R1 pad 1: Net-(U23-A) -> UH
- R1 pad 2: RX+ -> GND2
- R10 pad 1: BOOT -> RX+
- R10 pad 2: GND2 -> Net-(R10-Pad2)
- R11 pad 1: Net-(D3-A) -> TX+
- R11 pad 2: +3.3V -> Net-(R11-Pad2)
- R12 pad 1: Net-(D4-A) -> Net-(U5-Y)
- R12 pad 2: +3.3V -> TX+
- R13 pad 1: Net-(D5-A) -> Net-(U5-Z)
- R13 pad 2: +3.3V -> TX-
- R14 pad 1: Net-(D6-A) -> Net-(U5-B)
- R14 pad 2: +3.3V -> RX-
- R18 pad 1: UH -> Net-(D8-A)
- R18 pad 2: GND2 -> STO FBK 24V
- R19 pad 1: VH -> Net-(R17-Pad2)
- R19 pad 2: GND2 -> Net-(R19-Pad2)
- R2 pad 1: Net-(U23-B) -> VH
- R2 pad 2: RX- -> GND2
- R20 pad 1: WH -> STO CH1 FIELD
- R20 pad 2: GND2 -> Net-(R20-Pad2)
- R21 pad 1: UL -> Net-(R20-Pad2)
- R21 pad 2: GND2 -> Net-(D6-K)
- R22 pad 1: VL -> STO CH2 FIELD
- R22 pad 2: GND2 -> Net-(R22-Pad2)
- R23 pad 1: WL -> Net-(R22-Pad2)
- R23 pad 2: GND2 -> Net-(D7-K)
- R24 pad 1: HEATSINK_TEMP_1_ADC -> Net-(D7-K)
- R24 pad 2: GND2 -> Net-(U11-A)
- R25 pad 1: UM -> Net-(D6-K)
- R25 pad 2: UM_ADC -> Net-(U10-A)
- R26 pad 1: UM_ADC -> Net-(D7-K)
- R26 pad 2: GND2 -> Net-(U11-A)
- R27 pad 1: VM -> Net-(D6-K)
- R27 pad 2: VM_ADC -> Net-(U10-A)
- R28 pad 1: VM_ADC -> Net-(R28-Pad1)
- R28 pad 2: GND2 -> +3.3V
- R29 pad 1: WM -> Net-(R29-Pad1)
- R29 pad 2: WM_ADC -> +3.3V
- R3 pad 1: Net-(U23-Z) -> WH
- R3 pad 2: TX- -> GND2
- R30 pad 1: WM_ADC -> STO CH1 MCU FBK
- R30 pad 2: GND2 -> Net-(R30-Pad2)
- R33 pad 1: +15V -> Net-(R31-Pad2)
- R33 pad 2: Net-(D16-A) -> STO CH2
- R34 pad 1: VBUS -5V -> +3.3V
- R34 pad 2: Net-(D18-K) -> STO CH1
- R35 pad 1: Net-(D16-K) -> +3.3V
- R35 pad 2: Net-(D19-K) -> STO CH2
- R36 pad 1: Net-(U10-OUTA) -> +15V
- R36 pad 2: Net-(Q1-G) -> Net-(D9-A)
- R37 pad 1: HEATSINK_TEMP_2_ADC -> +15V
- R37 pad 2: GND2 -> Net-(D10-A)
- R38 pad 1: U -> VBUS -5V
- R38 pad 2: U_ADC -> Net-(D11-K)
- R39 pad 1: U_ADC -> VBUS -5V
- R39 pad 2: GND2 -> Net-(D12-K)
- R4 pad 1: Net-(U23-Y) -> UL
- R4 pad 2: TX+ -> GND2
- R40 pad 1: V -> Net-(D9-K)
- R40 pad 2: V_ADC -> Net-(D13-K)
- R41 pad 1: V_ADC -> Net-(D10-K)
- R41 pad 2: GND2 -> Net-(D14-K)
- R42 pad 1: W -> Net-(U14-OUTA)
- R42 pad 2: W_ADC -> Net-(Q2-G)
- R43 pad 1: W_ADC -> Net-(U14-OUTB)
- R43 pad 2: GND2 -> Net-(Q3-G)
- R44 pad 1: +VDC -> Net-(U15-OUTA)
- R44 pad 2: VBUS_ADC -> Net-(Q4-G)
- R45 pad 1: VBUS_ADC -> Net-(U15-OUTB)
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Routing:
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- added copper zone on F.Cu, net (none)
- added copper zone on F.Cu, net DCBUS+
- added copper zone on In1.Cu, net DCBUS+
- added copper zone on F.Cu, net DCBUS-
- added copper zone on In2.Cu, net DCBUS-
- added copper zone on F.Cu, net Net-(D13-A)
- added copper zone on F.Cu, net Net-(D14-A)
- added copper zone on F.Cu, net Net-(D17-A)
- added copper zone on F.Cu, net Net-(Q7-DS)
- added copper zone on F.Cu, net Net-(U14-OUTA)
- added copper zone on F.Cu, net Net-(U14-OUTB)
- added copper zone on F.Cu, net Net-(U15-OUTA)
- added copper zone on F.Cu, net Net-(U15-OUTB)
- added copper zone on F.Cu, net Net-(U18-OUTA)
- added copper zone on F.Cu, net Net-(U18-OUTB)
- added copper zone on B.Cu, net U
- added copper zone on F.Cu, net U_
- added copper zone on F.Cu, net V_
- added copper zone on F.Cu, net W_
- removed copper zone on F.Cu, net Net-(D19-A)
- removed copper zone on F.Cu, net Net-(D20-A)
- removed copper zone on F.Cu, net Net-(D24-A)
- removed copper zone on F.Cu, net Net-(Q1-DS)
- removed copper zone on F.Cu, net Net-(U10-OUTA)
- removed copper zone on F.Cu, net Net-(U10-OUTB)
- removed copper zone on F.Cu, net Net-(U11-OUTA)
- removed copper zone on F.Cu, net Net-(U11-OUTB)
- removed copper zone on F.Cu, net Net-(U13-OUTA)
- removed copper zone on F.Cu, net Net-(U13-OUTB)
- removed copper zone on F.Cu, net Net-(U6-SW)
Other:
- outline, holes or cut-outs redrawn
- board text added: "REV 2"
- board text removed: "24V"
- board text removed: "RX+"
- board text removed: "RX-"
- board text removed: "TX+"
- board text removed: "TX-"

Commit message: round PCb edges
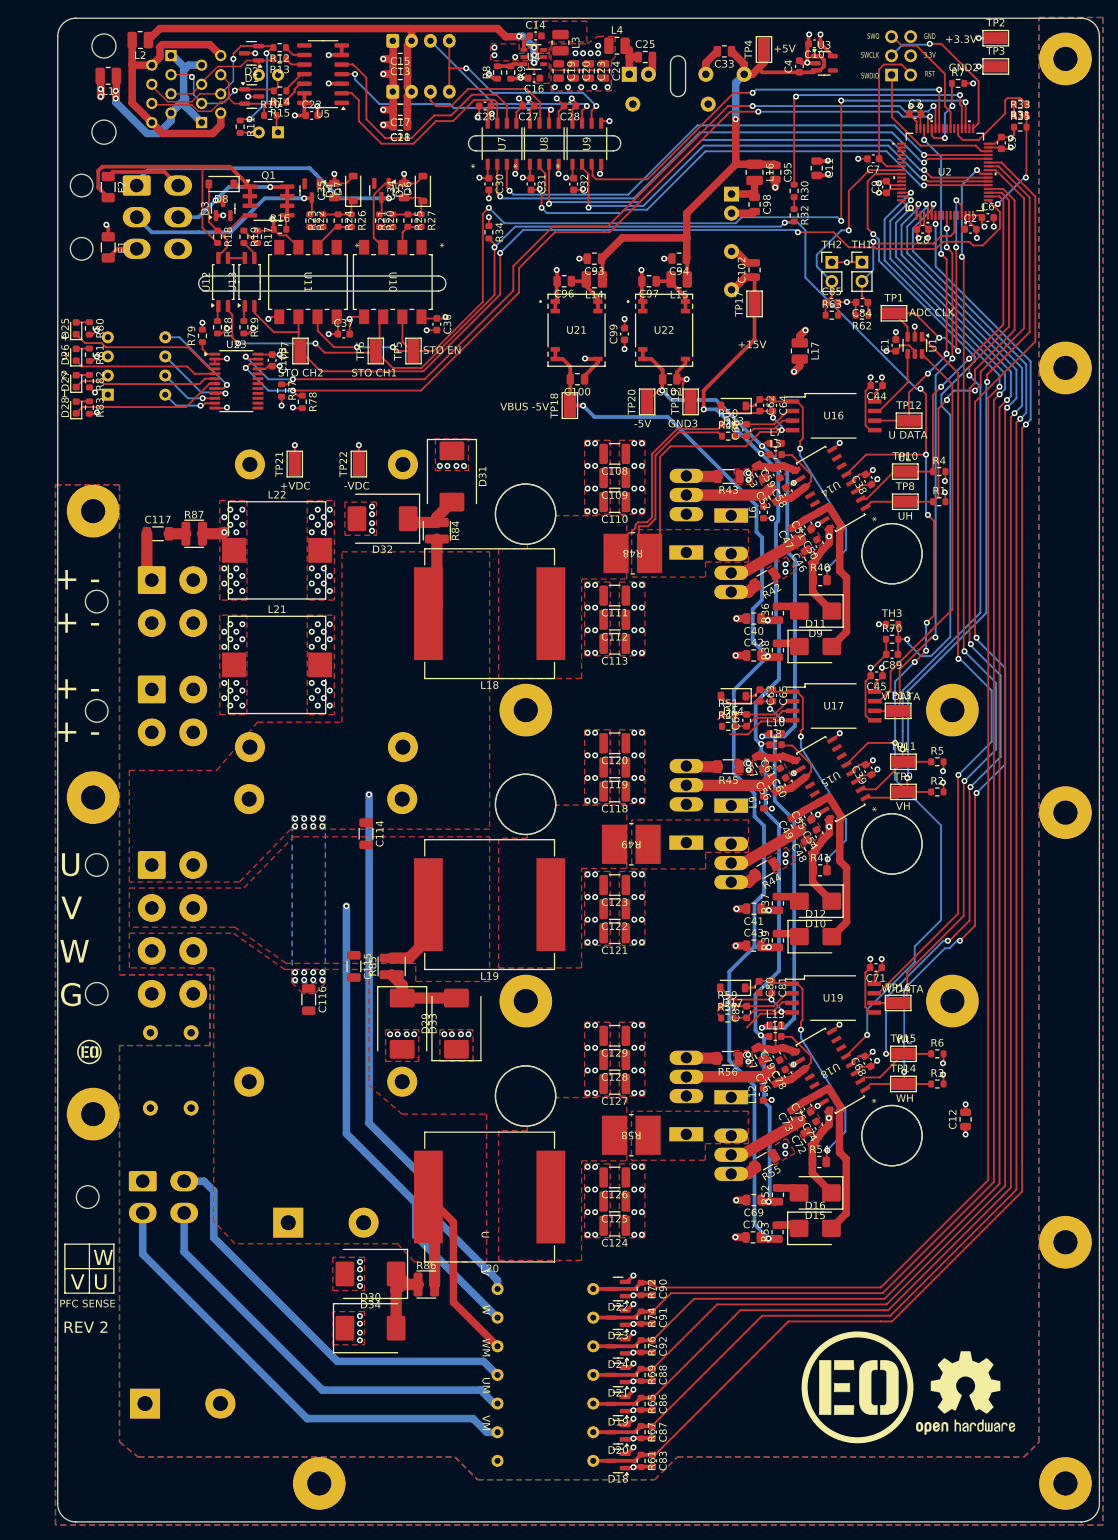
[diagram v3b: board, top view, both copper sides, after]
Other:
- board size 138.4 x 199.6 mm -> 138.2 x 199.5 mm
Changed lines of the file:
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@@
 		(layer "Edge.Cuts")
 	)
-	(gr_rect
-		(start 310.25 51.655628)
-		(end 448.622 251.269628)
+	(gr_line
+		(start 446.102944 251.102944)
+		(end 312.697056 251.102944)
 		(stroke
 			(width 0.1)
-			(type solid)
+			(type default)
 		)
-		(fill none)
 		(layer "Edge.Cuts")
 	)
@@
 		(layer "Edge.Cuts")
 	)
+	(gr_arc
+		(start 310.297056 54)
+		(mid 311 52.302944)
+		(end 312.697056 51.6)
+		(stroke
+			(width 0.1)
+			(type default)
+		)
+		(layer "Edge.Cuts")
+	)
 	(gr_line
 		(start 393.6 61)
 		(end 393.6 57.6)
+		(stroke
+			(width 0.1)
+			(type default)
+		)
+		(layer "Edge.Cuts")
+	)
+	(gr_arc
+		(start 446.102944 51.6)
+		(mid 447.8 52.302944)
+		(end 448.502944 54)
+		(stroke
+			(width 0.1)
+			(type default)
+		)
+		(layer "Edge.Cuts")
+	)
+	(gr_line
+		(start 310.297056 248.702944)
+		(end 310.297056 54)
+		(stroke
+			(width 0.1)
+			(type default)
+		)
+		(layer "Edge.Cuts")
+	)
+	(gr_arc
+		(start 448.502944 248.702944)
+		(mid 447.8 250.4)
+		(end 446.102944 251.102944)
+		(stroke
+			(width 0.1)
+			(type default)
+		)
+		(layer "Edge.Cuts")
+	)
+	(gr_arc
+		(start 312.697056 251.102944)
+		(mid 311 250.4)
+		(end 310.297056 248.702944)
 		(stroke
 			(width 0.1)
@@
 		(start 330 87.8)
 		(end 360.8 87.8)
+		(stroke
+			(width 0.1)
+			(type default)
+		)
+		(layer "Edge.Cuts")
+	)
+	(gr_line
+		(start 312.697056 51.6)
+		(end 446.102944 51.6)
 		(stroke
 			(width 0.1)
@@
 		(stroke
 			(width 0.1)
+			(type default)
+		)
+		(layer "Edge.Cuts")
+	)
+	(gr_line
+		(start 448.502944 54)
+		(end 448.502944 248.702944)
+		(stroke
+			(width 0.1)
